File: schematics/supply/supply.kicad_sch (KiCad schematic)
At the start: 13 parts, among them J1 Conn_01x02_Pin, J2 RFShield_OnePiece, J3 RFShield_OnePiece, J4 Conn_01x01_Pin, J5 RFShield_OnePiece, J6 RFShield_OnePiece

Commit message: Board#1 schematics rewrited
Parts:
- removed H1 (x6): MountingHole, MountingHole:MountingHole_2.2mm_M2, symbol Mechanical:MountingHole
- removed J1: Conn_01x02_Pin, Connector_Wire:SolderWire-1.5sqmm_1x02_P6mm_D1.7mm_OD3mm, symbol Connector:Conn_01x02_Pin
- removed J3, J5, J6: RFShield_OnePiece, Library:EMI_SHIELD_1P_2H, symbol Device:RFShield_OnePiece
- removed J4: Conn_01x01_Pin, Connector_Wire:SolderWire-1.5sqmm_1x01_D1.7mm_OD3.9mm, symbol Connector:Conn_01x01_Pin
- added C1: 1000 uF@16V, Capacitor_THT:CP_Radial_D10.0mm_P5.00mm, symbol Device:C_Polarized
- added C2: 22 uF, Capacitor_SMD:C_1210_3225Metric, symbol Device:C
- added C3, C4: 100 nF, Capacitor_SMD:C_0603_1608Metric, symbol Device:C
- added C5, C6: 1 uF, Capacitor_SMD:C_0603_1608Metric, symbol Device:C
- added J1: power +5V connector from board#1, Connector_Wire:SolderWire-1.5sqmm_1x02_P6mm_D1.7mm_OD3mm, symbol Connector:Conn_01x02_Socket
- added J2: VSYS connector from Board#1, Connector_JST:JST_XH_B4B-XH-A_1x04_P2.50mm_Vertical, symbol Connector:Conn_01x04_Socket
- added NT1: PWR2LOGIC, NetTie:NetTie-2_SMD_Pad0.5mm, symbol Device:NetTie_2
- added Q1: IRLML0030, Package_TO_SOT_SMD:SOT-23, symbol Transistor_FET:IRLML0030
- added R1: ?, Resistor_SMD:R_0805_2012Metric, symbol Device:R
- added R2: 350, Resistor_SMD:R_0805_2012Metric, symbol Device:R
- added U1: ISO1540, Package_SO:SOIC-8_3.9x4.9mm_P1.27mm, symbol Isolator:ISO1540
- added U2: 6N137, Package_DIP:DIP-8_W7.62mm, symbol Isolator:6N137
- added U3: FAN3100, Package_TO_SOT_SMD:SOT-23-5, symbol My_Library:FAN3100
- renumbered J2 to J3
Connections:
- net Control & Fan/SIGNAL_OUT: now also Q1.1 (G)
- net GND renamed VSYS_GND
- net VSYS_GND: now also C4.2, J2.4 (Pin_4), Q1.2 (S), U1.5 (GND2)
- new net: R1.1, U2.2 (A)
- new net: R2.2, U2.6 (VO), U3.4 (IN-)
- new net: Q1.3 (D), U2.3 (C)
- new net +5V_PWR_GND: C1.2, C2.1, C3.2, C5.2, C6.2, J1.2 (Pin_2), U1.4 (GND1), U2.5 (GND), U3.2 (GND)
- new net +5V_PWR_LOGIC: C1.1, C2.2, C3.1, NT1.2, U1.1 (VCC1)
- new net +5V_PWR_VCC: C5.1, C6.1, J1.1 (Pin_1), NT1.1, R2.1, U2.7 (EN), U2.8 (VCC), U3.1 (VCC), U3.3 (IN+)
- new net Output connectors/SIGNAL_OUT: U3.5 (OUT)
- new net PWR_SCL: U1.3 (SCL1)
- new net PWR_SDA: U1.2 (SDA1)
- new net VSYS_SCL: J2.1 (Pin_1), U1.6 (SCL2)
- new net VSYS_SDA: J2.2 (Pin_2), U1.7 (SDA2)
- new net VSYS_VCC: C4.1, J2.3 (Pin_3), R1.2, U1.8 (VCC2)
- no-connect marks 0 -> 2
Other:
- sheet Internal 5V & out usb renamed usb ports
- removed sheet Power output
- sheet Control & Fan ports: added VSYS_GND, VSYS_VCC; removed +5V_VSYS, POWER_OUTPUT_CURRENT_SENSE, POWER_OUTPUT_FB, POWER_OUTPUT_SHUTDOWN#, POWER_OUTPUT_VOLT_SENSE
- sheet Output connectors ports: added +5V_GND, +5V_LOGIC, +5V_VCC; removed +3.3V_OUT, +5V_OUT, +5V_VSYS, POWER_OUT
- sheet usb ports ports: added +5V_GND, +5V_LOGIC, +5V_VCC; removed +3.3_VOUT, +5V_OUT, +5V_VSYS, 400V, V_STANDBY
- note added: "TODO: add more holes"
- note removed: "Holes on board#1"
- moved on the sheet: H1, J3

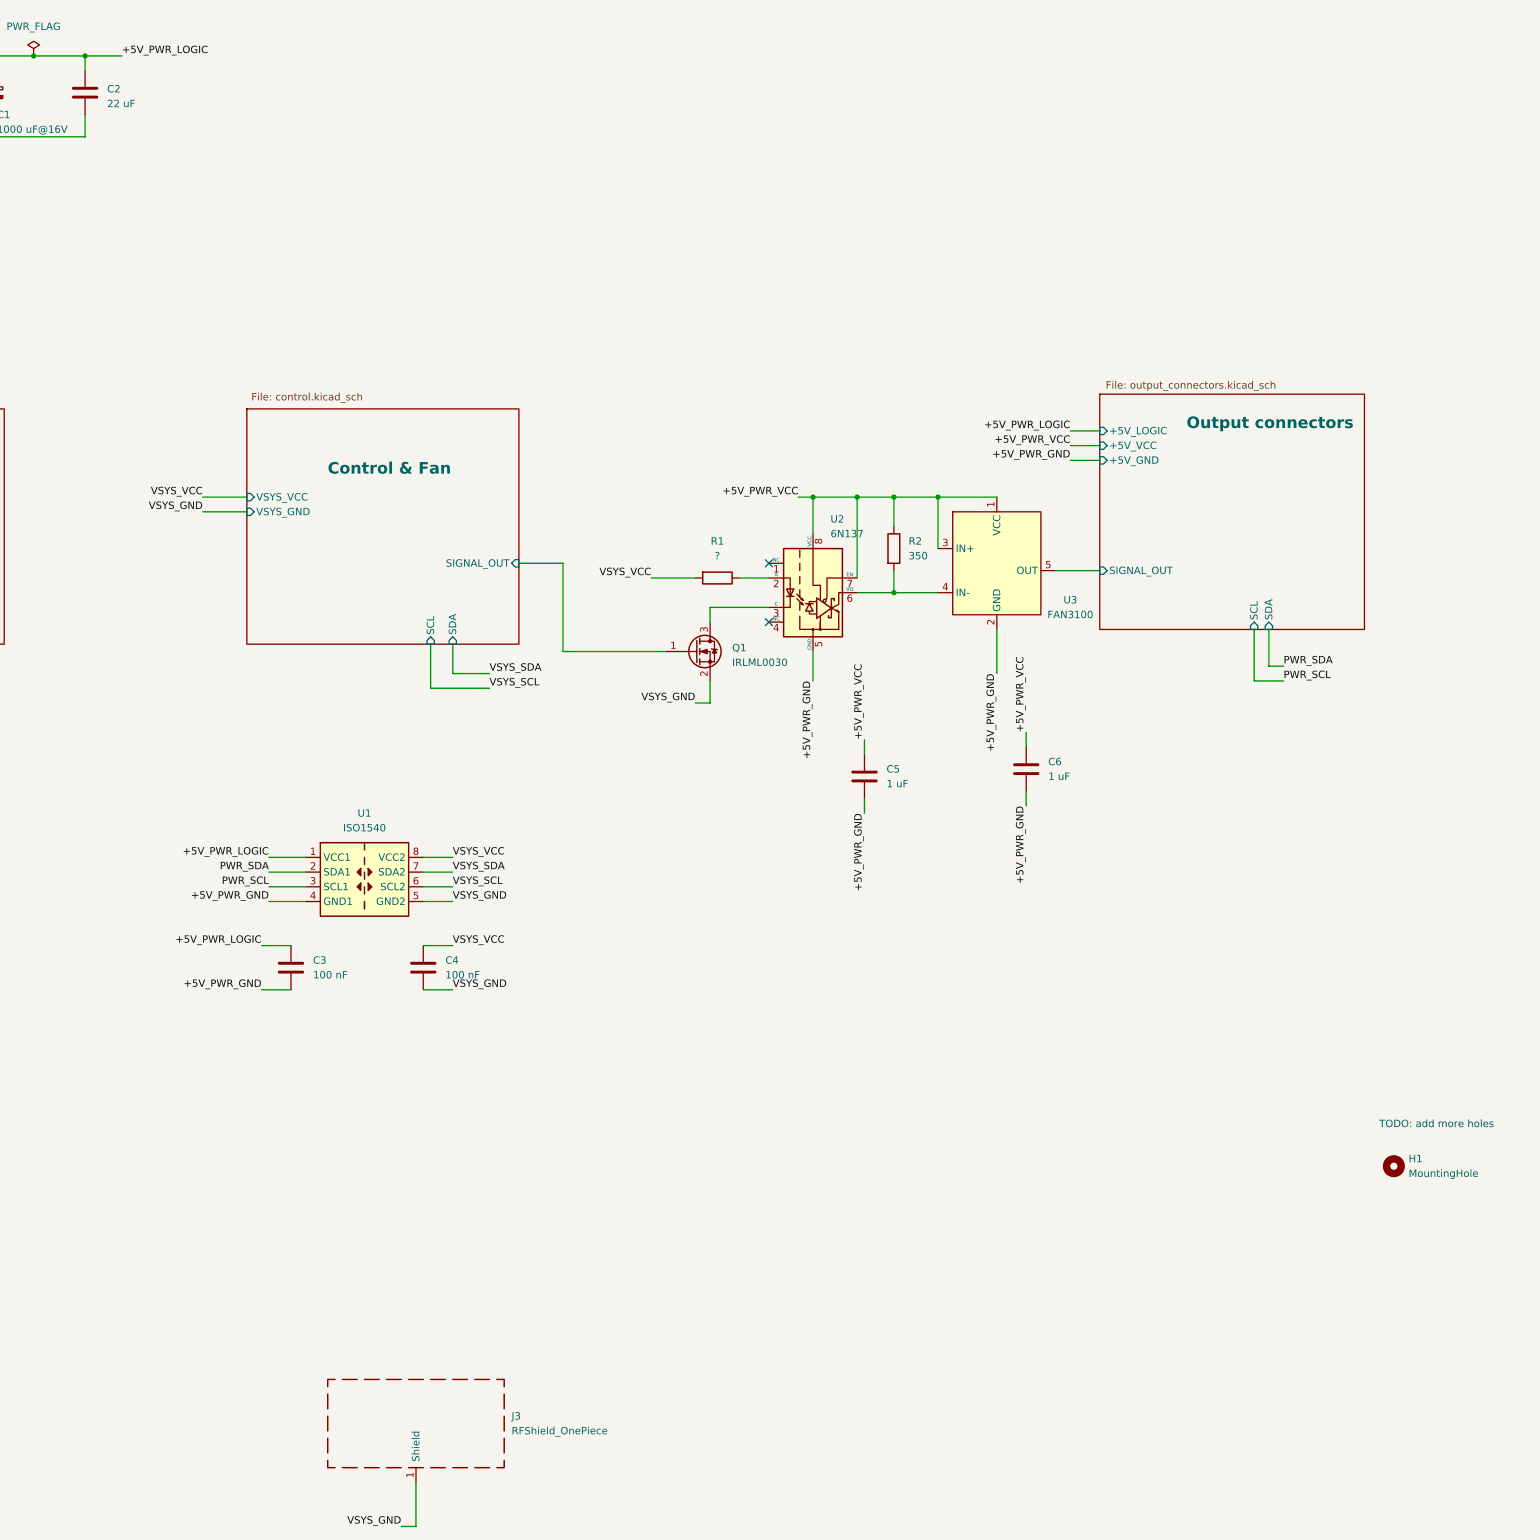
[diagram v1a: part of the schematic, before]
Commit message: first board routed
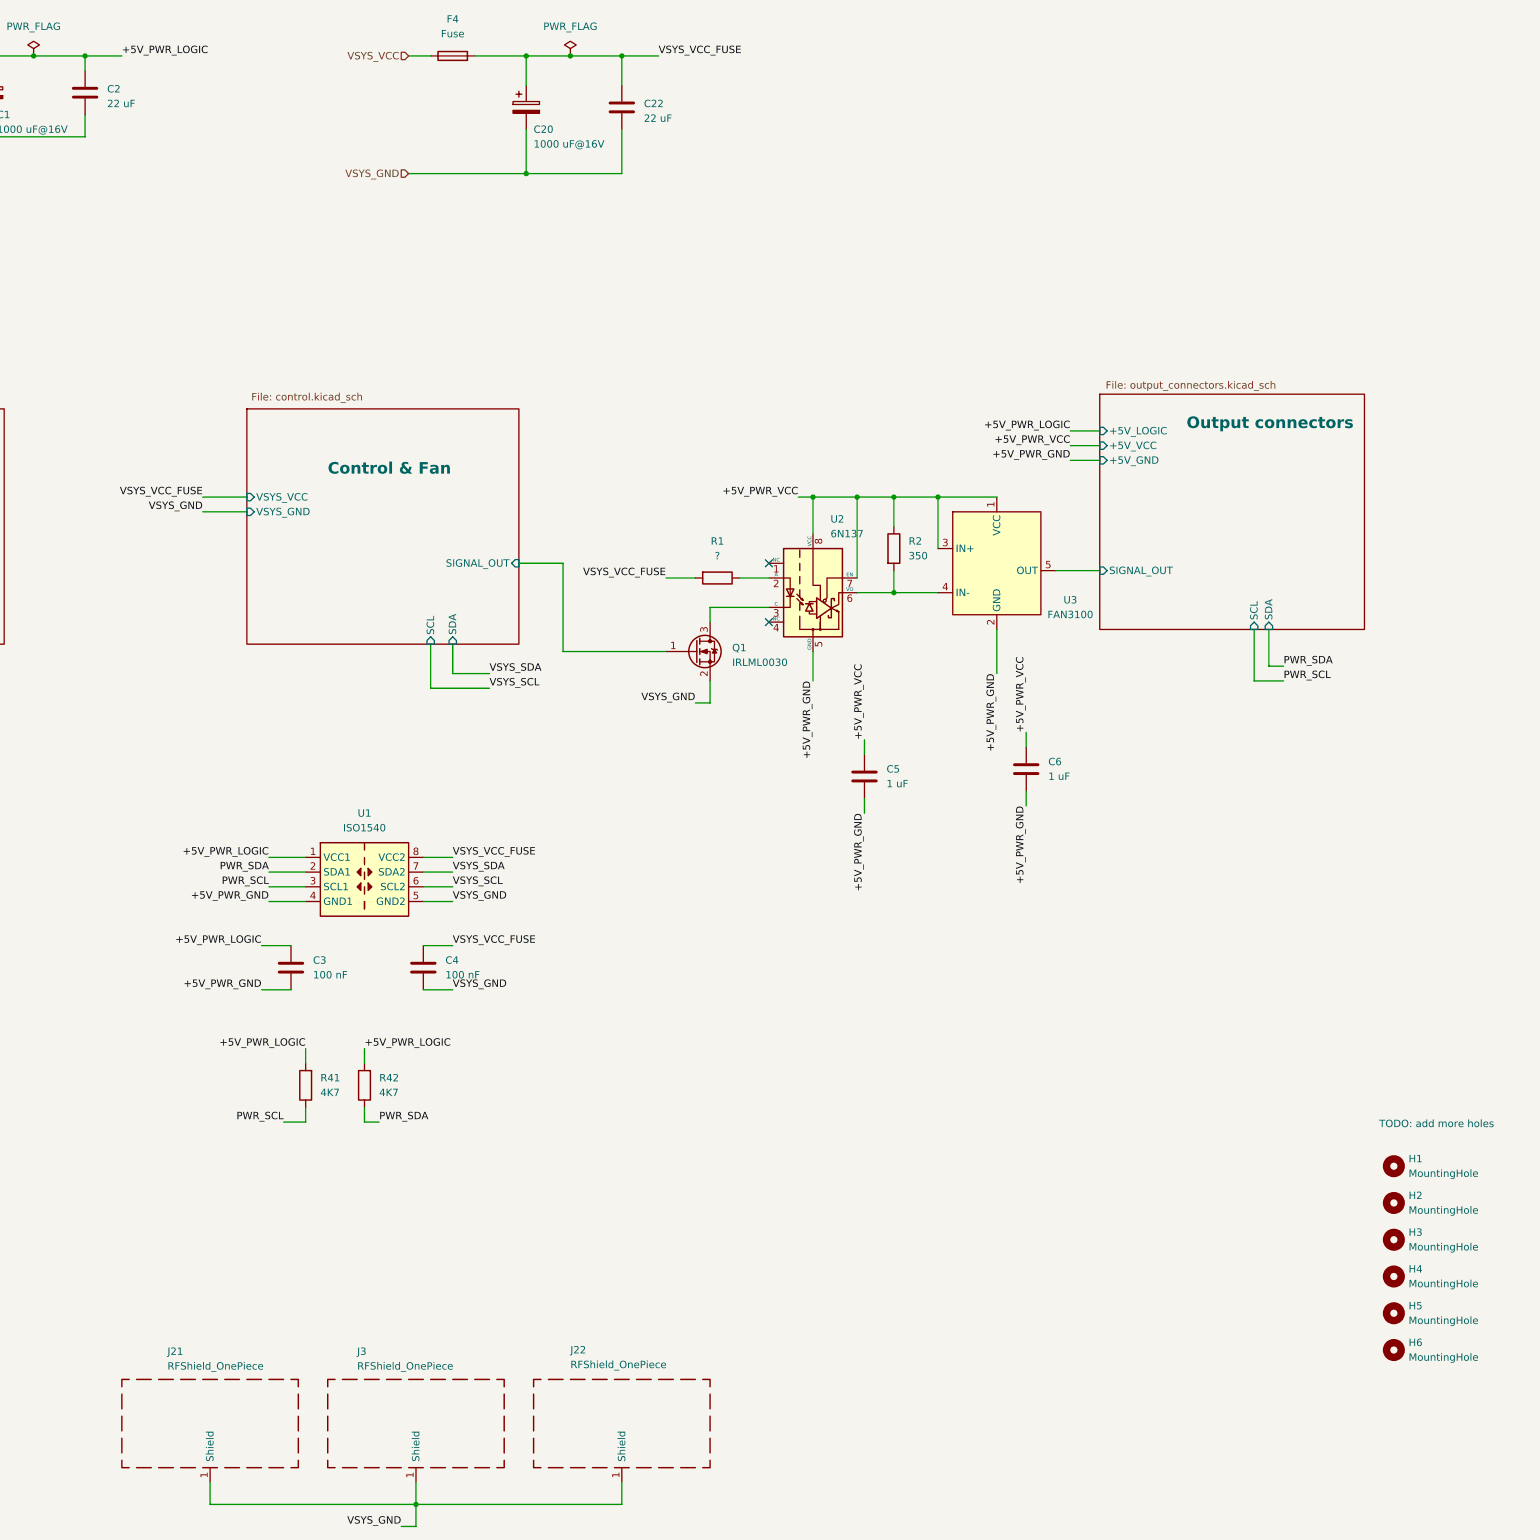
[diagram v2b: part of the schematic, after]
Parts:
- added C20: 1000 uF@16V, Capacitor_THT:CP_Radial_D10.0mm_P5.00mm, symbol Device:C_Polarized
- added C22: 22 uF, Capacitor_SMD:C_1210_3225Metric, symbol Device:C
- added F4: Fuse, Library:FuseHolder1808, symbol Device:Fuse
- added H2, H3, H4, H5, H6: MountingHole, MountingHole:MountingHole_2.2mm_M2, symbol Mechanical:MountingHole
- added J21, J22: RFShield_OnePiece, Library:EMI_SHIELD_1P_2H, symbol Device:RFShield_OnePiece
- added R41, R42: 4K7, Resistor_SMD:R_0805_2012Metric, symbol Device:R
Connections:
- net +5V_PWR_LOGIC: now also R41.2, R42.2
- net PWR_SCL: now also R41.1
- net PWR_SDA: now also R42.1
- net VSYS_GND: now also C20.2, C22.1, J21.1 (Shield), J22.1 (Shield)
- net VSYS_VCC: now also F4.1; no longer C4.1, R1.2, U1.8 (VCC2)
- new net VSYS_VCC_FUSE: C20.1, C22.2, C4.1, F4.2, R1.2, U1.8 (VCC2)
